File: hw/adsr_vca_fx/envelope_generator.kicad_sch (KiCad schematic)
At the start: 11 parts, among them J12 Conn_01x03, J6 Conn_02x05_Odd_Even, SW1 SW_Push, U3 STM32L432KBUx

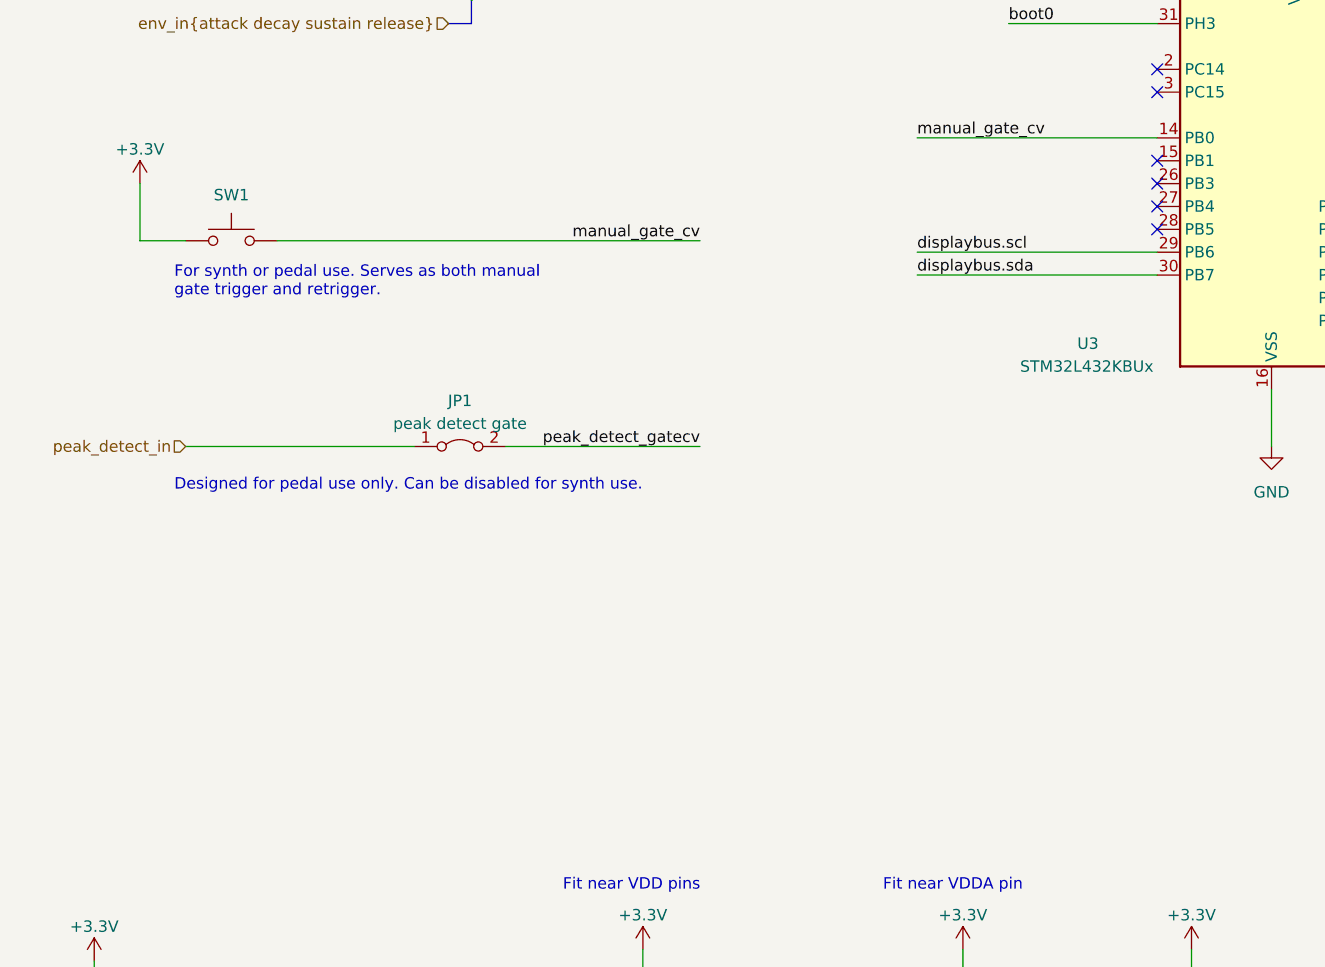
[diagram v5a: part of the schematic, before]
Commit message: updated layout
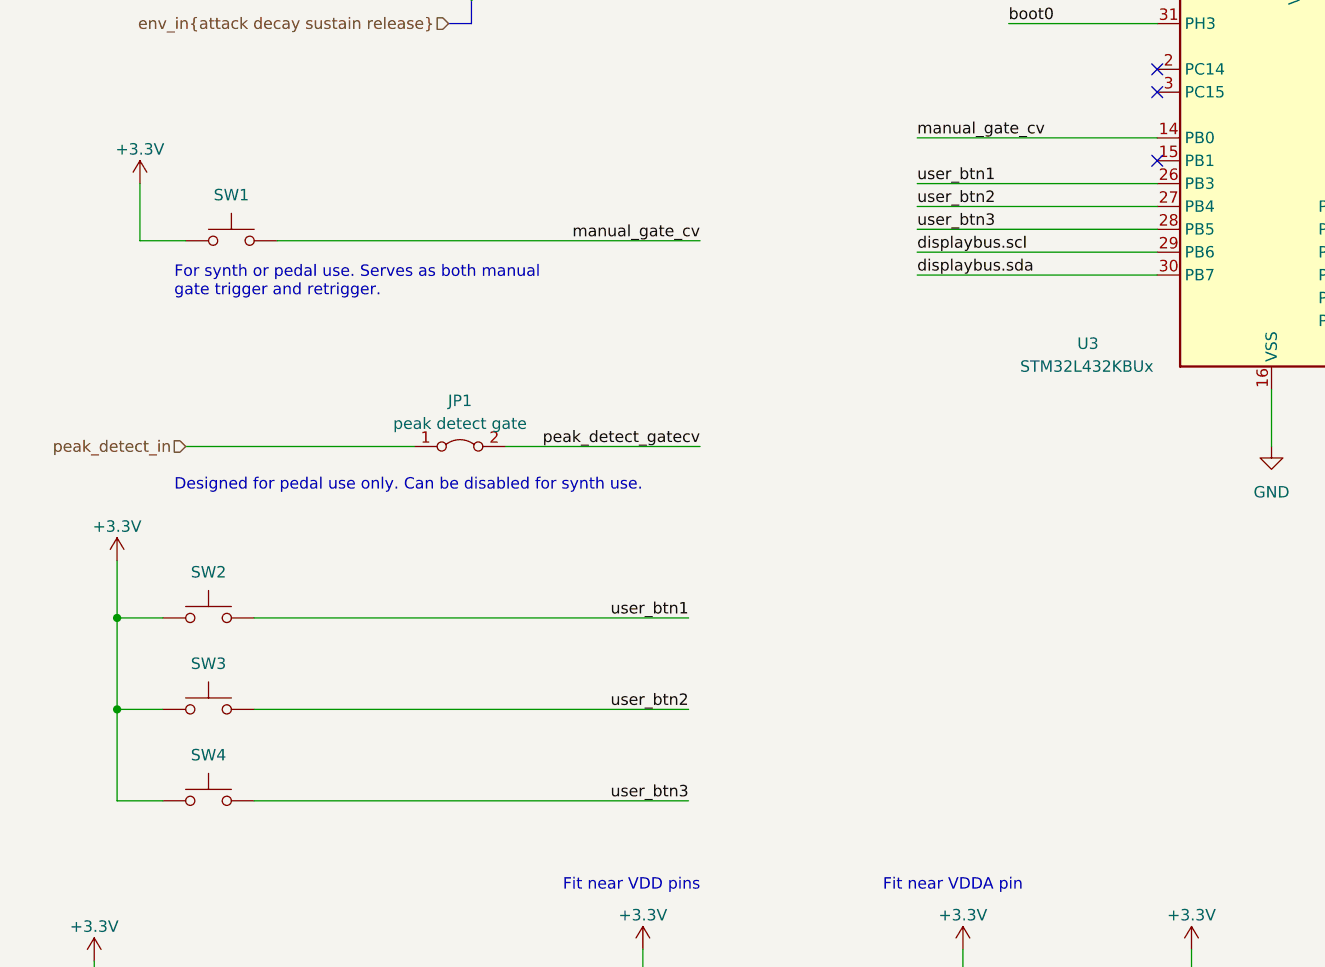
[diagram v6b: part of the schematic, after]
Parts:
- added SW2, SW3, SW4: SW_Push, Button_Switch_THT:SW_PUSH_6mm, symbol Switch:SW_Push
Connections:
- net +3.3V: now also SW2.1, SW3.1, SW4.1
- net user_btn1: now reaches U3.26 (PB3)
- net user_btn1: now also SW2.2
- net user_btn2: now reaches U3.27 (PB4)
- net user_btn2: now also SW3.2
- net user_btn3: now reaches U3.28 (PB5)
- net user_btn3: now also SW4.2
- no-connect marks 16 -> 13
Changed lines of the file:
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@@
   (junction (at 24.13 170.18) (diameter 0) (color 0 0 0 0)
   )
+  (junction (at 26.67 124.46) (diameter 0) (color 0 0 0 0)
+  )
   (junction (at 24.13 165.1) (diameter 0) (color 0 0 0 0)
   )
   (junction (at 85.09 172.72) (diameter 0) (color 0 0 0 0)
+  )
+  (junction (at 26.67 114.3) (diameter 0) (color 0 0 0 0)
   )
   (junction (at 120.65 172.72) (diameter 0) (color 0 0 0 0)
@@
   (no_connect (at 167.64 60.96))
   (no_connect (at 142.24 53.34))
-  (no_connect (at 142.24 68.58))
   (no_connect (at 167.64 63.5))
   (no_connect (at 142.24 63.5))
   (no_connect (at 45.72 167.64))
   (no_connect (at 167.64 66.04))
-  (no_connect (at 142.24 71.12))
   (no_connect (at 33.02 167.64))
   (no_connect (at 45.72 165.1))
-  (no_connect (at 142.24 66.04))
   (no_connect (at 142.24 55.88))
   (no_connect (at 167.64 73.66))
@@
     (stroke (width 0) (type default))
   )
+  (wire (pts (xy 26.67 114.3) (xy 26.67 107.95))
+    (stroke (width 0) (type default))
+  )
   (wire (pts (xy 198.12 53.34) (xy 167.64 53.34))
     (stroke (width 0) (type default))
@@
     (stroke (width 0) (type default))
   )
+  (wire (pts (xy 31.75 114.3) (xy 26.67 114.3))
+    (stroke (width 0) (type default))
+  )
   (wire (pts (xy 85.09 34.29) (xy 68.58 34.29))
     (stroke (width 0) (type default))
   )
+  (wire (pts (xy 26.67 124.46) (xy 31.75 124.46))
+    (stroke (width 0) (type default))
+  )
   (wire (pts (xy 73.66 172.72) (xy 85.09 172.72))
     (stroke (width 0) (type default))
@@
     (stroke (width 0) (type default))
   )
+  (wire (pts (xy 142.24 71.12) (xy 115.57 71.12))
+    (stroke (width 0) (type default))
+  )
   (wire (pts (xy 24.13 152.4) (xy 24.13 160.02))
     (stroke (width 0) (type default))
@@
     (stroke (width 0) (type default))
   )
+  (wire (pts (xy 41.91 134.62) (xy 90.17 134.62))
+    (stroke (width 0) (type default))
+  )
+  (wire (pts (xy 142.24 66.04) (xy 115.57 66.04))
+    (stroke (width 0) (type default))
+  )
   (wire (pts (xy 167.64 76.2) (xy 194.31 76.2))
     (stroke (width 0) (type default))
@@
     (stroke (width 0) (type default))
   )
+  (wire (pts (xy 41.91 114.3) (xy 90.17 114.3))
+    (stroke (width 0) (type default))
+  )
+  (wire (pts (xy 41.91 124.46) (xy 90.17 124.46))
+    (stroke (width 0) (type default))
+  )
   (wire (pts (xy 144.78 154.94) (xy 146.05 154.94))
     (stroke (width 0) (type default))
@@
     (stroke (width 0) (type default))
   )
+  (wire (pts (xy 26.67 114.3) (xy 26.67 124.46))
+    (stroke (width 0) (type default))
+  )
   (wire (pts (xy 144.78 157.48) (xy 162.56 157.48))
     (stroke (width 0) (type default))
@@
     (stroke (width 0) (type default))
   )
+  (wire (pts (xy 26.67 134.62) (xy 31.75 134.62))
+    (stroke (width 0) (type default))
+  )
   (wire (pts (xy 234.95 83.82) (xy 220.98 83.82))
     (stroke (width 0) (type default))
@@
     (stroke (width 0) (type default))
   )
+  (wire (pts (xy 142.24 68.58) (xy 115.57 68.58))
+    (stroke (width 0) (type default))
+  )
   (wire (pts (xy 45.72 162.56) (xy 57.15 162.56))
     (stroke (width 0) (type default))
@@
   )
   (wire (pts (xy 234.95 81.28) (xy 220.98 81.28))
+    (stroke (width 0) (type default))
+  )
+  (wire (pts (xy 26.67 124.46) (xy 26.67 134.62))
     (stroke (width 0) (type default))
   )
@@
     (effects (font (size 1.27 1.27)) (justify left bottom))
   )
+  (label "user_btn1" (at 90.17 114.3 180) (fields_autoplaced)
+    (effects (font (size 1.27 1.27)) (justify right bottom))
+  )
   (label "displaybus.sda" (at 115.57 76.2 0) (fields_autoplaced)
     (effects (font (size 1.27 1.27)) (justify left bottom))
   )
+  (label "user_btn2" (at 90.17 124.46 180) (fields_autoplaced)
+    (effects (font (size 1.27 1.27)) (justify right bottom))
+  )
   (label "env_in.release" (at 198.12 58.42 180) (fields_autoplaced)
     (effects (font (size 1.27 1.27)) (justify right bottom))
@@
     (effects (font (size 1.27 1.27)) (justify right bottom))
   )
+  (label "user_btn3" (at 115.57 71.12 0) (fields_autoplaced)
+    (effects (font (size 1.27 1.27)) (justify left bottom))
+  )
   (label "displaybus.sda" (at 220.98 83.82 0) (fields_autoplaced)
     (effects (font (size 1.27 1.27)) (justify left bottom))
@@
     (effects (font (size 1.27 1.27)) (justify right bottom))
   )
+  (label "user_btn1" (at 115.57 66.04 0) (fields_autoplaced)
+    (effects (font (size 1.27 1.27)) (justify left bottom))
+  )
   (label "swclk" (at 194.31 78.74 180) (fields_autoplaced)
     (effects (font (size 1.27 1.27)) (justify right bottom))
@@
   (label "boot0" (at 162.56 157.48 180) (fields_autoplaced)
     (effects (font (size 1.27 1.27)) (justify right bottom))
+  )
+  (label "user_btn3" (at 90.17 134.62 180) (fields_autoplaced)
+    (effects (font (size 1.27 1.27)) (justify right bottom))
+  )
+  (label "user_btn2" (at 115.57 68.58 0) (fields_autoplaced)
+    (effects (font (size 1.27 1.27)) (justify left bottom))
   )
   (label "adsr_env_out2" (at 222.25 57.15 0) (fields_autoplaced)
@@
     )
   )
+  (symbol (lib_id "Switch:SW_Push") (at 36.83 134.62 0) (unit 1)
+    (in_bom yes) (on_board yes) (dnp no)
+    (property "Reference" "SW4" (at 36.83 129.54 0)
+      (effects (font (size 1.27 1.27)))
+    )
+    (property "Value" "SW_Push" (at 36.83 130.81 0)
+      (effects (font (size 1.27 1.27)) hide)
+    )
+    (property "Footprint" "Button_Switch_THT:SW_PUSH_6mm" (at 36.83 129.54 0)
+      (effects (font (size 1.27 1.27)) hide)
+    )
+    (property "Datasheet" "~" (at 36.83 129.54 0)
+      (effects (font (size 1.27 1.27)) hide)
+    )
+    (pin "1")
+    (pin "2")
+    (instances
+      (project "adsr_vca_fx"
+        (path "/2c7cc946-dcca-4ffb-b6a0-bf0c9ddb491b/1d3f5b6b-6d64-41ce-b32c-1d62b69c11ca"
+          (reference "SW4") (unit 1)
+        )
+      )
+    )
+  )
   (symbol (lib_id "Switch:SW_Push") (at 39.37 72.39 0) (unit 1)
     (in_bom yes) (on_board yes) (dnp no)
@@
     )
   )
+  (symbol (lib_id "Switch:SW_Push") (at 36.83 124.46 0) (unit 1)
+    (in_bom yes) (on_board yes) (dnp no)
+    (property "Reference" "SW3" (at 36.83 119.38 0)
+      (effects (font (size 1.27 1.27)))
+    )
+    (property "Value" "SW_Push" (at 36.83 120.65 0)
+      (effects (font (size 1.27 1.27)) hide)
+    )
+    (property "Footprint" "Button_Switch_THT:SW_PUSH_6mm" (at 36.83 119.38 0)
+      (effects (font (size 1.27 1.27)) hide)
+    )
+    (property "Datasheet" "~" (at 36.83 119.38 0)
+      (effects (font (size 1.27 1.27)) hide)
+    )
+    (pin "1")
+    (pin "2")
+    (instances
+      (project "adsr_vca_fx"
+        (path "/2c7cc946-dcca-4ffb-b6a0-bf0c9ddb491b/1d3f5b6b-6d64-41ce-b32c-1d62b69c11ca"
+          (reference "SW3") (unit 1)
+        )
+      )
+    )
+  )
   (symbol (lib_id "power:+3.3V") (at 24.13 152.4 0) (unit 1)
     (in_bom yes) (on_board yes) (dnp no) (fields_autoplaced)
@@
         (path "/2c7cc946-dcca-4ffb-b6a0-bf0c9ddb491b/1d3f5b6b-6d64-41ce-b32c-1d62b69c11ca"
           (reference "#PWR032") (unit 1)
+        )
+      )
+    )
+  )
+  (symbol (lib_id "Switch:SW_Push") (at 36.83 114.3 0) (unit 1)
+    (in_bom yes) (on_board yes) (dnp no)
+    (property "Reference" "SW2" (at 36.83 109.22 0)
+      (effects (font (size 1.27 1.27)))
+    )
+    (property "Value" "SW_Push" (at 36.83 110.49 0)
+      (effects (font (size 1.27 1.27)) hide)
+    )
+    (property "Footprint" "Button_Switch_THT:SW_PUSH_6mm" (at 36.83 109.22 0)
+      (effects (font (size 1.27 1.27)) hide)
+    )
+    (property "Datasheet" "~" (at 36.83 109.22 0)
+      (effects (font (size 1.27 1.27)) hide)
+    )
+    (pin "1")
+    (pin "2")
+    (instances
+      (project "adsr_vca_fx"
+        (path "/2c7cc946-dcca-4ffb-b6a0-bf0c9ddb491b/1d3f5b6b-6d64-41ce-b32c-1d62b69c11ca"
+          (reference "SW2") (unit 1)
         )
       )
@@
         )
       )
+    )
+  )
+  (symbol (lib_id "power:+3.3V") (at 26.67 107.95 0) (unit 1)
+    (in_bom yes) (on_board yes) (dnp no) (fields_autoplaced)
+    (property "Reference" "#PWR070" (at 26.67 111.76 0)
+      (effects (font (size 1.27 1.27)) hide)
+    )
+    (property "Value" "+3.3V" (at 26.67 104.14 0)
+      (effects (font (size 1.27 1.27)))
+    )
+    (property "Footprint" "" (at 26.67 107.95 0)
+      (effects (font (size 1.27 1.27)) hide)
+    )
+    (property "Datasheet" "" (at 26.67 107.95 0)
+      (effects (font (size 1.27 1.27)) hide)
+    )
+    (pin "1")
+    (instances
+      (project "adsr_vca_fx"
+        (path "/2c7cc946-dcca-4ffb-b6a0-bf0c9ddb491b/1d3f5b6b-6d64-41ce-b32c-1d62b69c11ca"
+          (reference "#PWR070") (unit 1)
+        )
+      )
